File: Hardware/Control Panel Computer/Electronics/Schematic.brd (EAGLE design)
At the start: 108.9 x 80 mm, 16 parts, among them IC1 7805T, J1 1X2-3.5MM, J2 1X2-3.5MM, J3 1X2-3.5MM, J4 1X2-3.5MM, J5 1X2-3.5MM

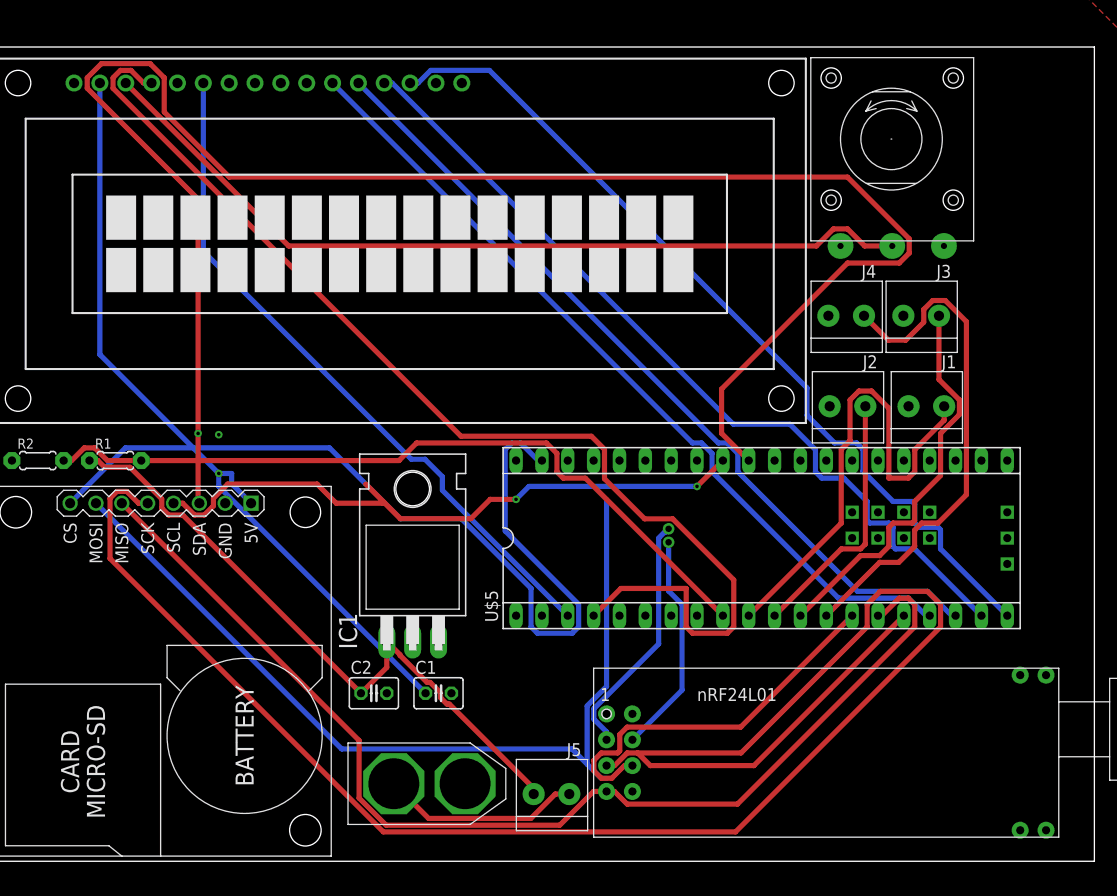
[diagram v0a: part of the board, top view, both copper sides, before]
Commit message: change control panel processor to STM32 Bluepill
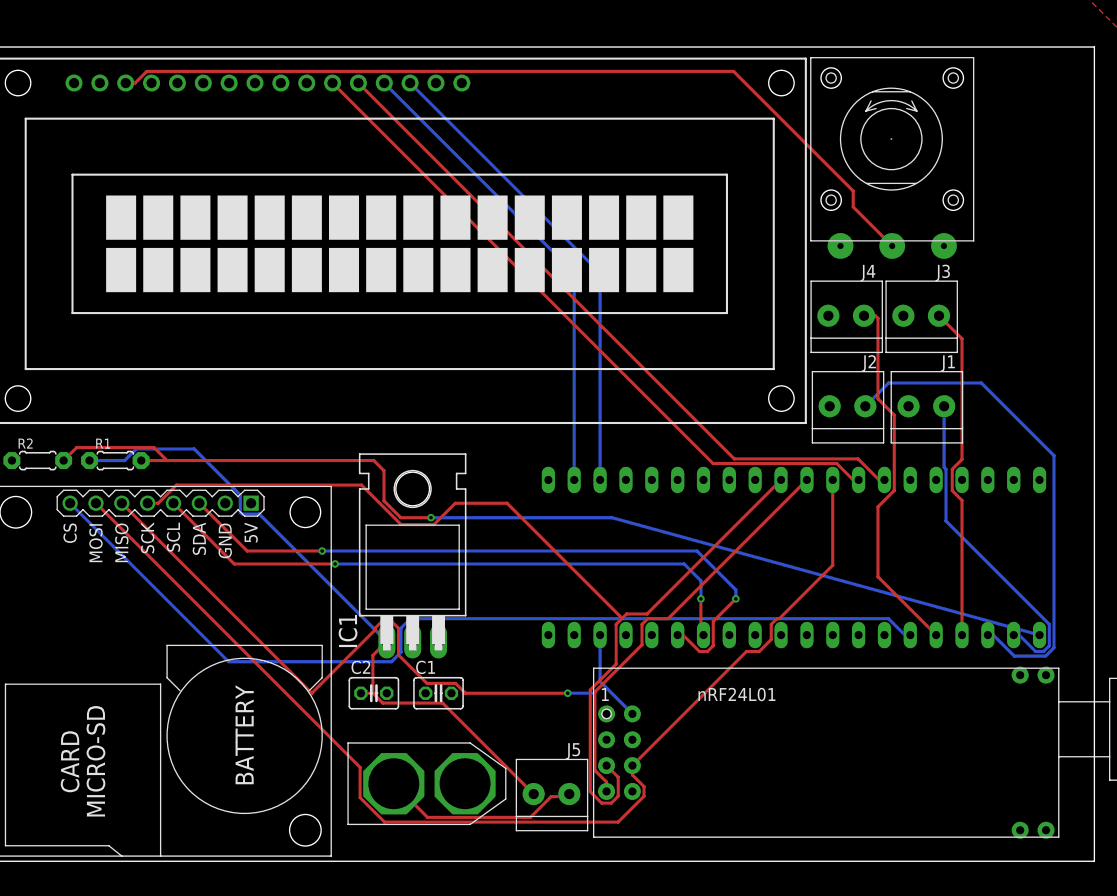
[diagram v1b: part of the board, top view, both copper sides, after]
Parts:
- removed U$5: ARDUINO-TEENSY++, teensypp:TEENSY++
- added U$6: (no value), BluePill:BLUE_PILL
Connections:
- removed net A1: U$5.B3
- removed net A2: U$5.A1
- removed net B1: U$5.B2
- removed net B2: U$5.A2
- removed net C1: U$5.B1
- removed net C2: U$5.A3
- removed net D1: U$5.B0
- removed net D2: U$5.A4
- removed net E1: U$5.D4
- removed net E2: U$5.A5
- removed net F1: U$5.D5
- removed net F2: U$5.A6
- removed net G1: U$5.A0
- removed net G2: U$5.A7
- net 5V: now also U$6.P$18; no longer U$5.+5V, U$5.5V
- net CE: no longer U$5.E4
- net CSN: no longer U$5.E5
- net DA4: now also U$6.P$28; no longer U$5.C4
- net DA5: now also U$6.P$27; no longer U$5.C5
- net DA6: now also U$6.P$39; no longer U$5.C6
- net DA7: now also U$6.P$38; no longer U$5.C7
- net EN: no longer U$5.D0
- net GND: now also U$6.P$21; no longer U$5.GND, U$5.GND2, U$5.GRND1
- net MISO: now also U$6.P$30; no longer U$5.C2
- net MOSI: now also U$6.P$29; no longer U$5.C1
- net RS: no longer U$5.D1
- net SCK: now also U$6.P$31; no longer U$5.C3
- net SCL: now also U$6.P$14; no longer U$5.E7
- net SDA: now also U$6.P$15; no longer U$5.E6
- net SDCS: now also U$6.P$6; no longer U$5.B6
- net SWITCH1: now also U$6.P$2; no longer U$5.D7
- net SWITCH2: now also U$6.P$3; no longer U$5.E0
- net SWITCH3: now also U$6.P$4; no longer U$5.E1
- net SWITCH4: now also U$6.P$5; no longer U$5.C0
- net VOLTAGE: now also U$6.P$1; no longer U$5.D6
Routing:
- net RS: track 112.1 -> 0.00 mm
- net SDA: track 170.3 -> 67.0 mm, vias 1 -> 2
- net SCK: track 188.2 -> 101.1 mm
- net 5V: track 78.2 -> 9.06 mm, vias 1 -> 0
- net EN: track 67.9 -> 0.00 mm
- net DA7: track 86.4 -> 46.7 mm
- net DA6: track 83.8 -> 46.7 mm
- net VOLTAGE: track 74.6 -> 105.1 mm, vias 0 -> 1
- net CE: track 24.3 -> 0.00 mm
- net SWITCH2: track 25.4 -> 49.0 mm
- net CSN: track 22.0 -> 0.00 mm
- net MOSI: track 126.0 -> 110.2 mm
- net SWITCH1: track 47.5 -> 32.2 mm
- net SWITCH4: track 50.9 -> 36.3 mm
- net DA4: track 81.4 -> 67.8 mm
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
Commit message: fix errors
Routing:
- net MISO: track 102.5 -> 111.1 mm
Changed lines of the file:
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@@
 <contactref element="U$2" pad="+"/>
 <contactref element="J5" pad="1"/>
-<wire x1="55.5206625" y1="6.35" x2="57.15" y2="6.35" width="0.3048" layer="1"/>
+<wire x1="57.15" y1="6.35" x2="55.5206625" y2="6.35" width="0.3048" layer="1"/>
 <wire x1="43.3728" y1="4.3072" x2="53.4778625" y2="4.3072" width="0.3048" layer="1"/>
 <wire x1="53.4778625" y1="4.3072" x2="55.5206625" y2="6.35" width="0.3048" layer="1"/>
 <wire x1="40.06" y1="7.62" x2="43.3728" y2="4.3072" width="0.3048" layer="1"/>
-<wire x1="57.15" y1="6.35" x2="57.299" y2="6.604" width="0" layer="19" extent="1-1"/>
+<wire x1="57.299" y1="6.604" x2="57.15" y2="6.455" width="0.3048" layer="1"/>
+<wire x1="57.15" y1="6.455" x2="57.15" y2="6.35" width="0.3048" layer="1"/>
 </signal>
 <signal name="VIN">
@@
 <wire x1="39.0906" y1="35.4081625" x2="40.7421625" y2="33.7566" width="0.3048" layer="1"/>
 <wire x1="38.1" y1="39.37" x2="39.0906" y2="38.3794" width="0.3048" layer="1"/>
-<wire x1="103.505" y1="22.225" x2="61.4934" y2="33.7566" width="0.3048" layer="16"/>
-<wire x1="43.7134" y1="33.7566" x2="61.4934" y2="33.7566" width="0.3048" layer="16"/>
+<wire x1="103.505" y1="22.225" x2="101.754515625" y2="23.975484375" width="0.3048" layer="16"/>
+<wire x1="101.754515625" y1="23.975484375" x2="66.120228125" y2="33.7566" width="0.3048" layer="16"/>
+<wire x1="43.7134" y1="33.7566" x2="66.120228125" y2="33.7566" width="0.3048" layer="16"/>
 <wire x1="39.0906" y1="38.3794" x2="39.0906" y2="35.4081625" width="0.3048" layer="1"/>
 <wire x1="40.7421625" y1="33.7566" x2="43.7134" y2="33.7566" width="0.3048" layer="1"/>
@@
 <via x="57.15" y="16.51" extent="1-16" drill="0.35"/>
 <wire x1="47.085" y1="16.51" x2="57.15" y2="16.51" width="0.3048" layer="1"/>
-<wire x1="57.15" y1="16.51" x2="59.69" y2="16.51" width="0.3048" layer="16"/>
-<wire x1="59.69" y1="16.51" x2="59.817" y2="16.637" width="0" layer="19" extent="1-16"/>
+<wire x1="57.15" y1="16.51" x2="57.15" y2="10.668" width="0.3048" layer="16"/>
+<wire x1="57.15" y1="10.668" x2="60.96" y2="6.858" width="0.3048" layer="16"/>
 </signal>
 <signal name="SCK">
